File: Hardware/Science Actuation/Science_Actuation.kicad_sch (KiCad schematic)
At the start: 110 parts, among them J2 RJ45_LED_Shielded, Q1 BSS138, Q10 AO3401A, Q9 BSS138, SW1 SW_Push, SW10 SW_SPDT, SW2 SW_Push, SW3 SW_Push, SW4 SW_Push, SW5 SW_Push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

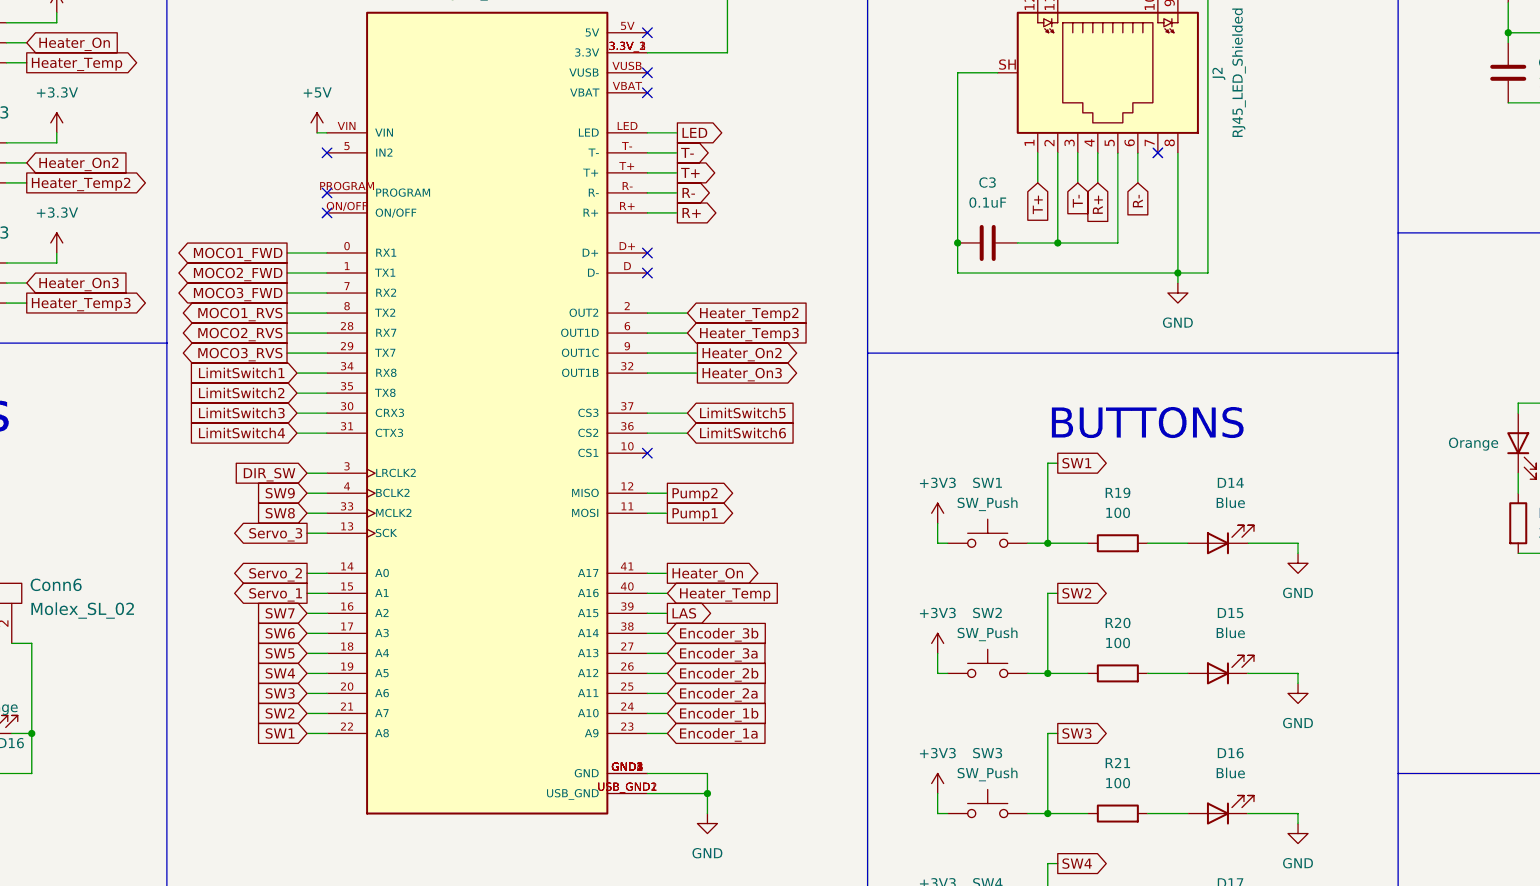
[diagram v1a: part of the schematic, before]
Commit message: Added traces and changed the layout of the board
Some of it is a mess and will probably be revised later
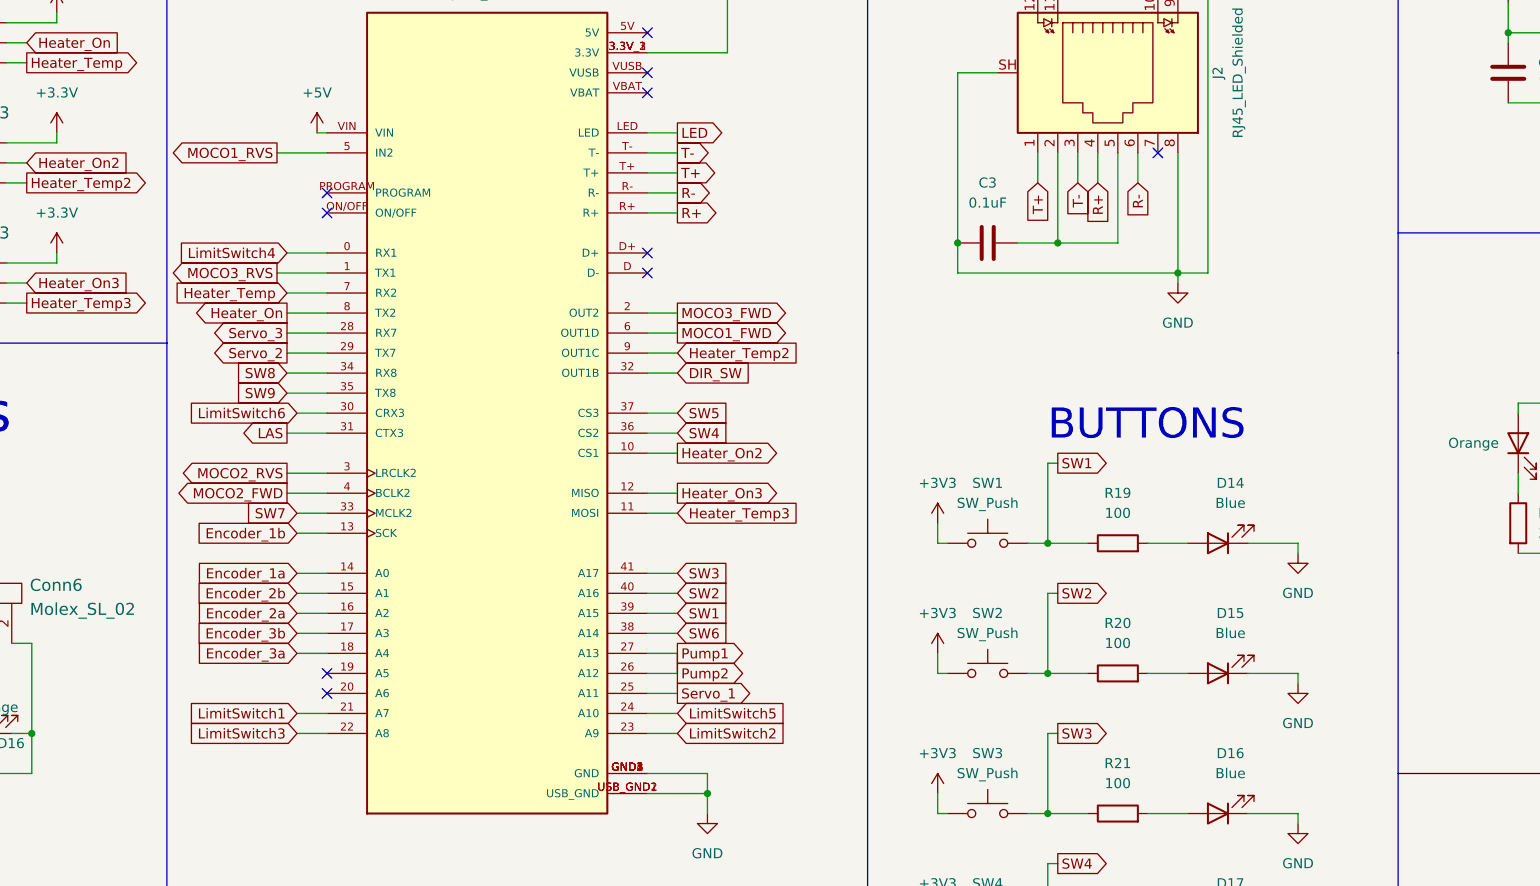
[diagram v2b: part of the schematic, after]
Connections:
- net DIR_SW: now also U2.32 (OUT1B); no longer U2.3 (LRCLK2)
- net Encoder_1a: now also U2.14 (A0); no longer U2.23 (A9)
- net Encoder_1b: now also U2.13 (SCK); no longer U2.24 (A10)
- net Encoder_2a: now also U2.16 (A2); no longer U2.25 (A11)
- net Encoder_2b: now also U2.15 (A1); no longer U2.26 (A12)
- net Encoder_3a: now also U2.18 (A4); no longer U2.27 (A13)
- net Encoder_3b: now also U2.17 (A3); no longer U2.38 (A14)
- net Heater_On: now also U2.8 (TX2); no longer U2.41 (A17)
- net Heater_On2: now also U2.10 (CS1); no longer U2.9 (OUT1C)
- net Heater_On3: now also U2.12 (MISO); no longer U2.32 (OUT1B)
- net Heater_Temp: now also U2.7 (RX2); no longer U2.40 (A16)
- net Heater_Temp2: now also U2.9 (OUT1C); no longer U2.2 (OUT2)
- net Heater_Temp3: now also U2.11 (MOSI); no longer U2.6 (OUT1D)
- net LAS: now also U2.31 (CTX3); no longer U2.39 (A15)
- net LimitSwitch1: now also U2.21 (A7); no longer U2.34 (RX8)
- net LimitSwitch2: now also U2.23 (A9); no longer U2.35 (TX8)
- net LimitSwitch3: now also U2.22 (A8); no longer U2.30 (CRX3)
- net LimitSwitch4: now also U2.0 (RX1); no longer U2.31 (CTX3)
- net LimitSwitch5: now also U2.24 (A10); no longer U2.37 (CS3)
- net LimitSwitch6: now also U2.30 (CRX3); no longer U2.36 (CS2)
- net MOCO1_FWD: now also U2.6 (OUT1D); no longer U2.0 (RX1)
- net MOCO1_RVS: now also U2.5 (IN2); no longer U2.8 (TX2)
- net MOCO2_FWD: now also U2.4 (BCLK2); no longer U2.1 (TX1)
- net MOCO2_RVS: now also U2.3 (LRCLK2); no longer U2.28 (RX7)
- net MOCO3_FWD: now also U2.2 (OUT2); no longer U2.7 (RX2)
- net MOCO3_RVS: now also U2.1 (TX1); no longer U2.29 (TX7)
- net Pump1: now also Q9.1 (G), R36.1, U2.26 (A12), U2.27 (A13); no longer U2.11 (MOSI)
- net SW1: now also U2.39 (A15); no longer U2.22 (A8)
- net SW2: now also U2.40 (A16); no longer U2.21 (A7)
- net SW3: now also U2.41 (A17); no longer U2.20 (A6)
- net SW4: now also U2.36 (CS2); no longer U2.19 (A5)
- net SW5: now also U2.37 (CS3); no longer U2.18 (A4)
- net SW6: now also U2.38 (A14); no longer U2.17 (A3)
- net SW7: now also U2.33 (MCLK2); no longer U2.16 (A2)
- net SW8: now also U2.34 (RX8); no longer U2.33 (MCLK2)
- net SW9: now also U2.35 (TX8); no longer U2.4 (BCLK2)
- net Servo_1: now also U2.25 (A11); no longer U2.15 (A1)
- net Servo_2: now also U2.29 (TX7); no longer U2.14 (A0)
- net Servo_3: now also U2.28 (RX7); no longer U2.13 (SCK)
- removed net Pump2: Q9.1 (G), R36.1, U2.12 (MISO)

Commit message: Temporary state
Removed things. Added a motor. WIP
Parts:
- added Conn17: Molex_SL_03, MRDT_Connectors:MOLEX_SL_03_Vertical, symbol MRDT_Connectors:Molex_SL_03
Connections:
- net +3.3V is gone; now on net +3V3: Conn14.3, Conn15.3, Conn16.3
- net +3V3: now also Conn17.1
- net MOCO3_FWD: now also U2.20 (A6)
- net MOCO3_RVS: now also U2.38 (A14)
- net Pump1: no longer Q9.1 (G), R36.1, U2.26 (A12)
- net SW6: now also U2.19 (A5); no longer U2.38 (A14)
- new net MOCO4_FWD: Conn17.2
- new net MOCO4_RVS: Conn17.3
- new net Pump2: Q9.1 (G), R36.1, U2.26 (A12)
- no-connect marks 12 -> 10
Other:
- moved on the sheet: Conn3, Conn4, Conn5, Conn6, Conn7, Conn8, D16, D2, D3, D4, D5, D6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

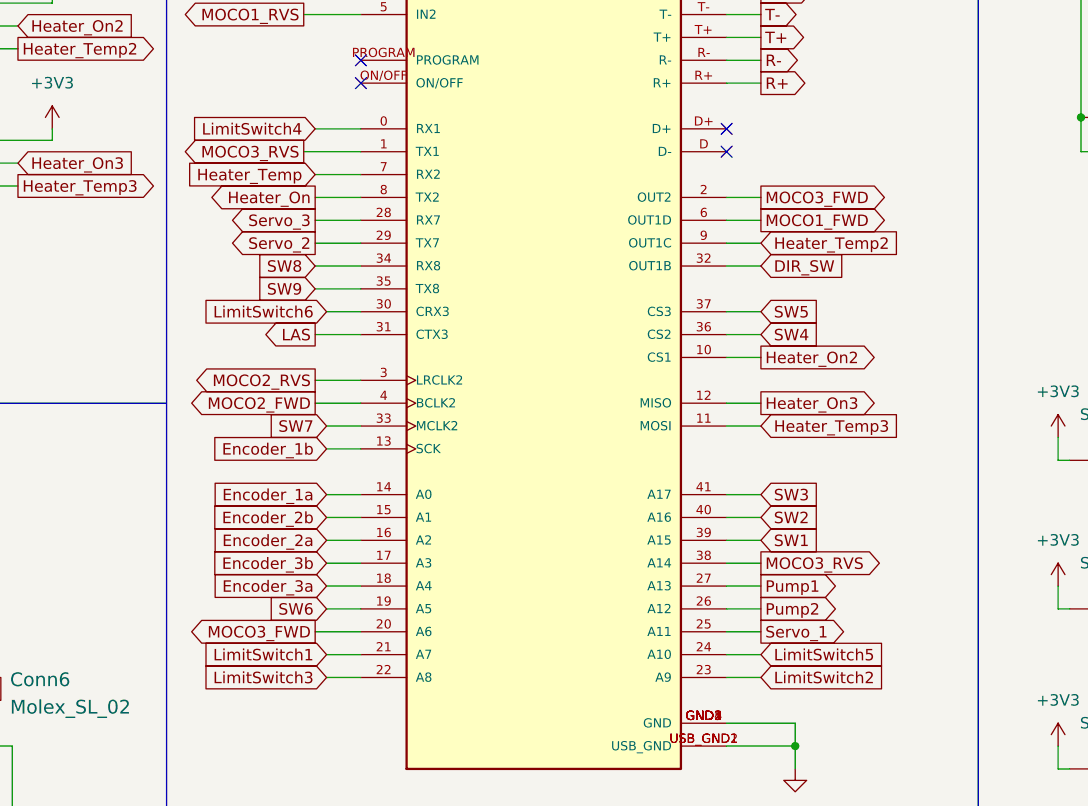
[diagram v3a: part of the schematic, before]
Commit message: Tried  Cleaning Up Board
Changed layout, added fourth MOCO Breakout
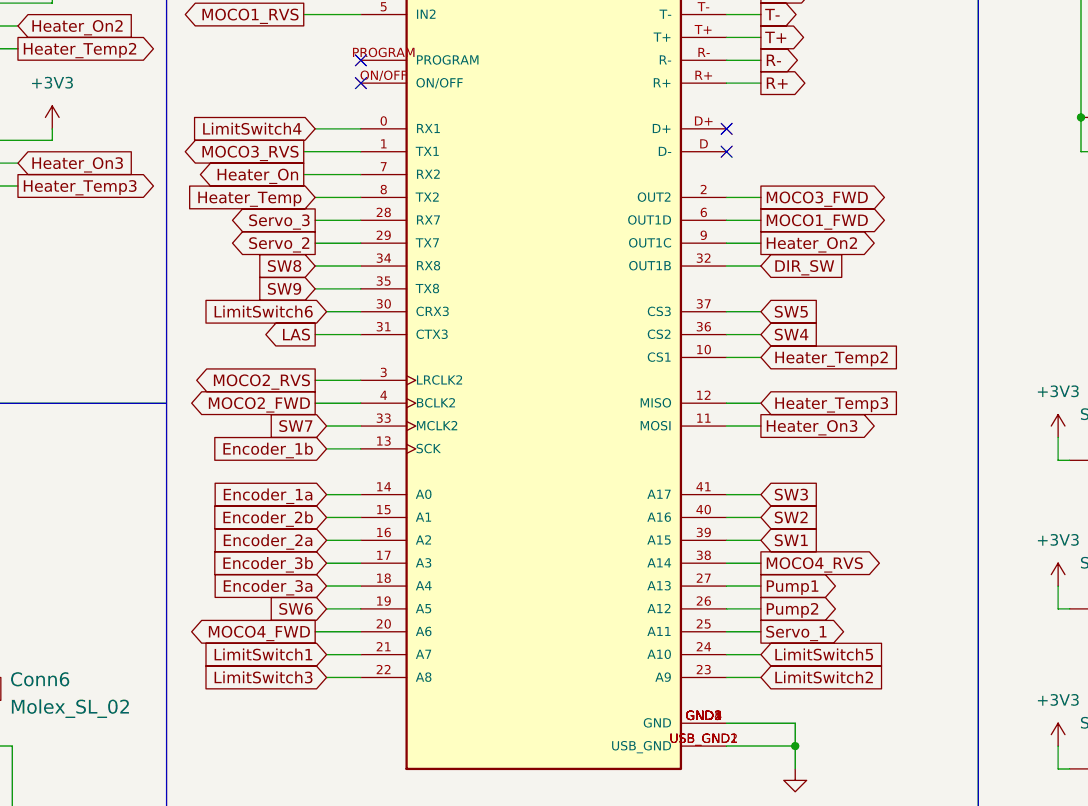
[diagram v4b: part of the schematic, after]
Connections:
- net Heater_On: now also U2.7 (RX2); no longer U2.8 (TX2)
- net Heater_On2: now also U2.9 (OUT1C); no longer U2.10 (CS1)
- net Heater_On3: now also U2.11 (MOSI); no longer U2.12 (MISO)
- net Heater_Temp: now also U2.8 (TX2); no longer U2.7 (RX2)
- net Heater_Temp2: now also U2.10 (CS1); no longer U2.9 (OUT1C)
- net Heater_Temp3: now also U2.12 (MISO); no longer U2.11 (MOSI)
- net MOCO3_FWD: no longer U2.20 (A6)
- net MOCO3_RVS: no longer U2.38 (A14)
- net MOCO4_FWD: now also U2.20 (A6)
- net MOCO4_RVS: now also U2.38 (A14)
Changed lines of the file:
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@@
     (stroke (width 0) (type default))
   )
-  (wire (pts (xy 168.91 73.66) (xy 173.99 73.66))
-    (stroke (width 0) (type default))
-  )
   (wire (pts (xy 172.72 199.39) (xy 176.53 199.39))
     (stroke (width 0) (type default))
@@
     (stroke (width 0) (type default))
   )
+  (wire (pts (xy 214.63 81.28) (xy 218.44 81.28))
+    (stroke (width 0) (type default))
+  )
   (wire (pts (xy 262.89 139.7) (xy 265.43 139.7))
     (stroke (width 0) (type default))
@@
     (stroke (width 0) (type default))
   )
+  (wire (pts (xy 168.91 76.2) (xy 173.99 76.2))
+    (stroke (width 0) (type default))
+  )
   (wire (pts (xy 55.88 137.16) (xy 50.8 137.16))
     (stroke (width 0) (type default))
@@
     (stroke (width 0) (type default))
   )
-  (wire (pts (xy 214.63 81.28) (xy 218.44 81.28))
-    (stroke (width 0) (type default))
-  )
   (wire (pts (xy 111.76 178.435) (xy 111.76 179.07))
     (stroke (width 0) (type default))
@@
     (stroke (width 0) (type default))
   )
+  (wire (pts (xy 214.63 101.6) (xy 218.44 101.6))
+    (stroke (width 0) (type default))
+  )
   (wire (pts (xy 278.13 191.77) (xy 283.21 191.77))
     (stroke (width 0) (type default))
@@
     (stroke (width 0) (type default))
   )
+  (wire (pts (xy 214.63 99.06) (xy 218.44 99.06))
+    (stroke (width 0) (type default))
+  )
   (wire (pts (xy 103.505 200.66) (xy 111.76 200.66))
     (stroke (width 0) (type default))
@@
     (stroke (width 0) (type default))
   )
-  (wire (pts (xy 214.63 93.98) (xy 218.44 93.98))
-    (stroke (width 0) (type default))
-  )
   (wire (pts (xy 251.46 175.26) (xy 252.73 175.26))
     (stroke (width 0) (type default))
@@
     (stroke (width 0) (type default))
   )
-  (wire (pts (xy 168.91 76.2) (xy 173.99 76.2))
-    (stroke (width 0) (type default))
-  )
   (polyline (pts (xy 242.57 151.13) (xy 242.57 256.54))
     (stroke (width 0) (type default))
@@
     (stroke (width 0) (type default))
   )
+  (wire (pts (xy 214.63 93.98) (xy 218.44 93.98))
+    (stroke (width 0) (type default))
+  )
   (wire (pts (xy 168.91 83.82) (xy 173.99 83.82))
     (stroke (width 0) (type default))
@@
     (stroke (width 0) (type default))
   )
-  (wire (pts (xy 214.63 99.06) (xy 218.44 99.06))
-    (stroke (width 0) (type default))
-  )
   (wire (pts (xy 214.63 129.54) (xy 218.44 129.54))
     (stroke (width 0) (type default))
   )
-  (wire (pts (xy 214.63 101.6) (xy 218.44 101.6))
-    (stroke (width 0) (type default))
-  )
   (wire (pts (xy 265.43 175.26) (xy 270.51 175.26))
     (stroke (width 0) (type default))
@@
     (stroke (width 0) (type default))
   )
+  (wire (pts (xy 167.64 73.66) (xy 173.99 73.66))
+    (stroke (width 0) (type default))
+  )
   (text "LIMIT SWITCH CONNECTORS" (at 95.25 109.22 0)
     (effects (font (size 3.81 3.81)) (justify right bottom))
@@
     )
   )
-  (global_label "MOCO3_FWD" (shape output) (at 168.91 124.46 180) (fields_autoplaced)
+  (global_label "MOCO4_FWD" (shape output) (at 168.91 124.46 180) (fields_autoplaced)
     (effects (font (size 1.27 1.27)) (justify right))
     (property "Intersheetrefs" "${INTERSHEET_REFS}" (at 154.5553 124.46 0)
@@
     )
   )
-  (global_label "Heater_On" (shape output) (at 168.91 76.2 180) (fields_autoplaced)
+  (global_label "Heater_On" (shape output) (at 167.64 73.66 180) (fields_autoplaced)
     (effects (font (size 1.27 1.27)) (justify right))
-    (property "Intersheetrefs" "${INTERSHEET_REFS}" (at 156.3091 76.2 0)
+    (property "Intersheetrefs" "${INTERSHEET_REFS}" (at 155.0391 73.66 0)
       (effects (font (size 1.27 1.27)) (justify right) hide)
     )
@@
     )
   )
-  (global_label "Heater_On2" (shape output) (at 218.44 93.98 0) (fields_autoplaced)
+  (global_label "Heater_On2" (shape output) (at 218.44 81.28 0) (fields_autoplaced)
     (effects (font (size 1.27 1.27)) (justify left))
-    (property "Intersheetrefs" "${INTERSHEET_REFS}" (at 232.2504 93.98 0)
+    (property "Intersheetrefs" "${INTERSHEET_REFS}" (at 232.2504 81.28 0)
       (effects (font (size 1.27 1.27)) (justify left) hide)
     )
   )
-  (global_label "Heater_Temp2" (shape input) (at 218.44 81.28 0) (fields_autoplaced)
+  (global_label "Heater_Temp2" (shape input) (at 218.44 93.98 0) (fields_autoplaced)
     (effects (font (size 1.27 1.27)) (justify left))
-    (property "Intersheetrefs" "${INTERSHEET_REFS}" (at 234.6694 81.28 0)
+    (property "Intersheetrefs" "${INTERSHEET_REFS}" (at 234.6694 93.98 0)
       (effects (font (size 1.27 1.27)) (justify left) hide)
     )
@@
     )
   )
-  (global_label "Heater_Temp" (shape input) (at 168.91 73.66 180) (fields_autoplaced)
+  (global_label "Heater_Temp" (shape input) (at 168.91 76.2 180) (fields_autoplaced)
     (effects (font (size 1.27 1.27)) (justify right))
-    (property "Intersheetrefs" "${INTERSHEET_REFS}" (at 153.8901 73.66 0)
+    (property "Intersheetrefs" "${INTERSHEET_REFS}" (at 153.8901 76.2 0)
       (effects (font (size 1.27 1.27)) (justify right) hide)
     )
@@
     )
   )
-  (global_label "Heater_Temp3" (shape input) (at 218.44 101.6 0) (fields_autoplaced)
+  (global_label "Heater_Temp3" (shape input) (at 218.44 99.06 0) (fields_autoplaced)
     (effects (font (size 1.27 1.27)) (justify left))
-    (property "Intersheetrefs" "${INTERSHEET_REFS}" (at 234.6694 101.6 0)
+    (property "Intersheetrefs" "${INTERSHEET_REFS}" (at 234.6694 99.06 0)
       (effects (font (size 1.27 1.27)) (justify left) hide)
     )
@@
     )
   )
-  (global_label "Heater_On3" (shape output) (at 218.44 99.06 0) (fields_autoplaced)
+  (global_label "Heater_On3" (shape output) (at 218.44 101.6 0) (fields_autoplaced)
     (effects (font (size 1.27 1.27)) (justify left))
-    (property "Intersheetrefs" "${INTERSHEET_REFS}" (at 232.2504 99.06 0)
+    (property "Intersheetrefs" "${INTERSHEET_REFS}" (at 232.2504 101.6 0)
       (effects (font (size 1.27 1.27)) (justify left) hide)
     )
@@
     )
   )
-  (global_label "MOCO3_RVS" (shape output) (at 218.44 116.84 0) (fields_autoplaced)
+  (global_label "MOCO4_RVS" (shape output) (at 218.44 116.84 0) (fields_autoplaced)
     (effects (font (size 1.27 1.27)) (justify left))
     (property "Intersheetrefs" "${INTERSHEET_REFS}" (at 232.5528 116.84 0)
@@
   )
   (symbol (lib_id "MRDT_Connectors:Molex_SL_03") (at 128.27 68.58 180) (unit 1)
-    (in_bom yes) (on_board yes) (dnp no) (fields_autoplaced)
+    (in_bom yes) (on_board yes) (dnp no)
     (property "Reference" "Conn16" (at 127 63.5 0)
       (effects (font (size 1.524 1.524)))
